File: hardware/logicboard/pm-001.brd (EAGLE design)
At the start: 45 x 45 mm, 18 parts, among them K1 G5V1, T1 2SC1815

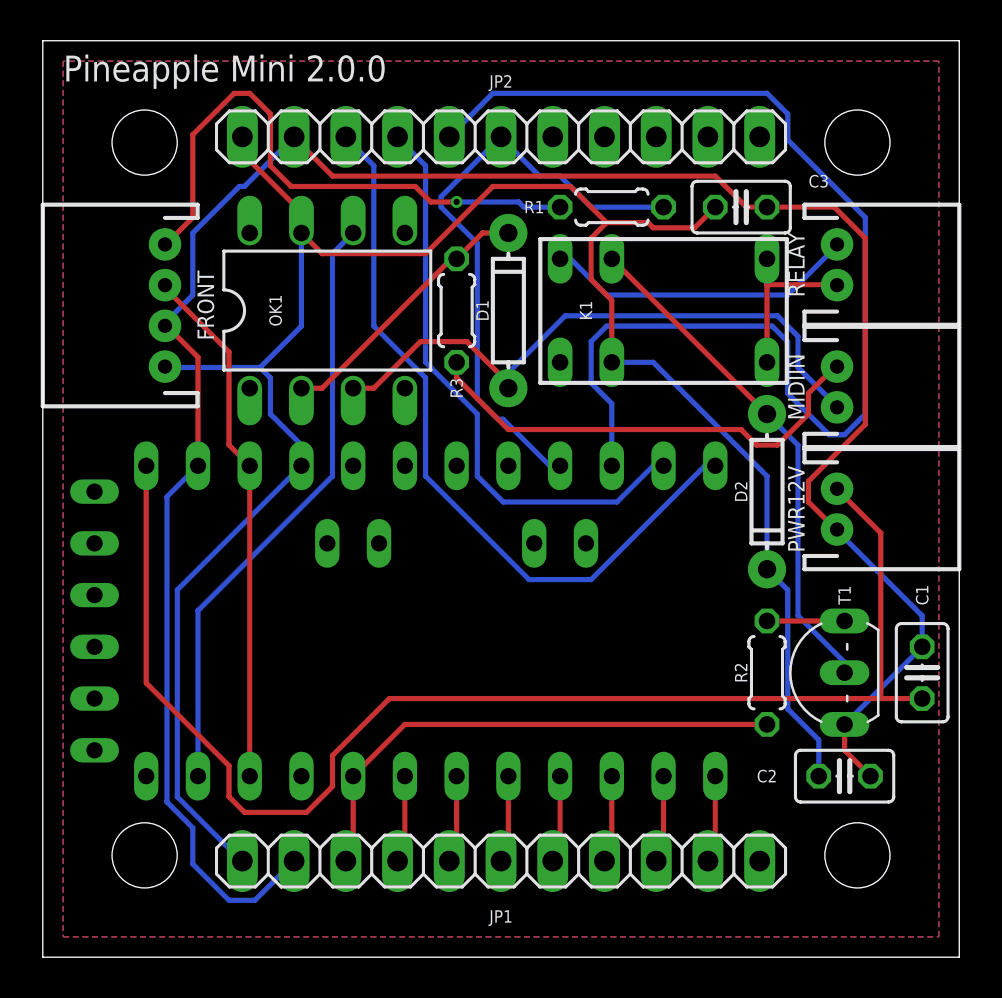
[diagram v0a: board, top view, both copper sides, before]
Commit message: Moved FTDI connector to stackable position.
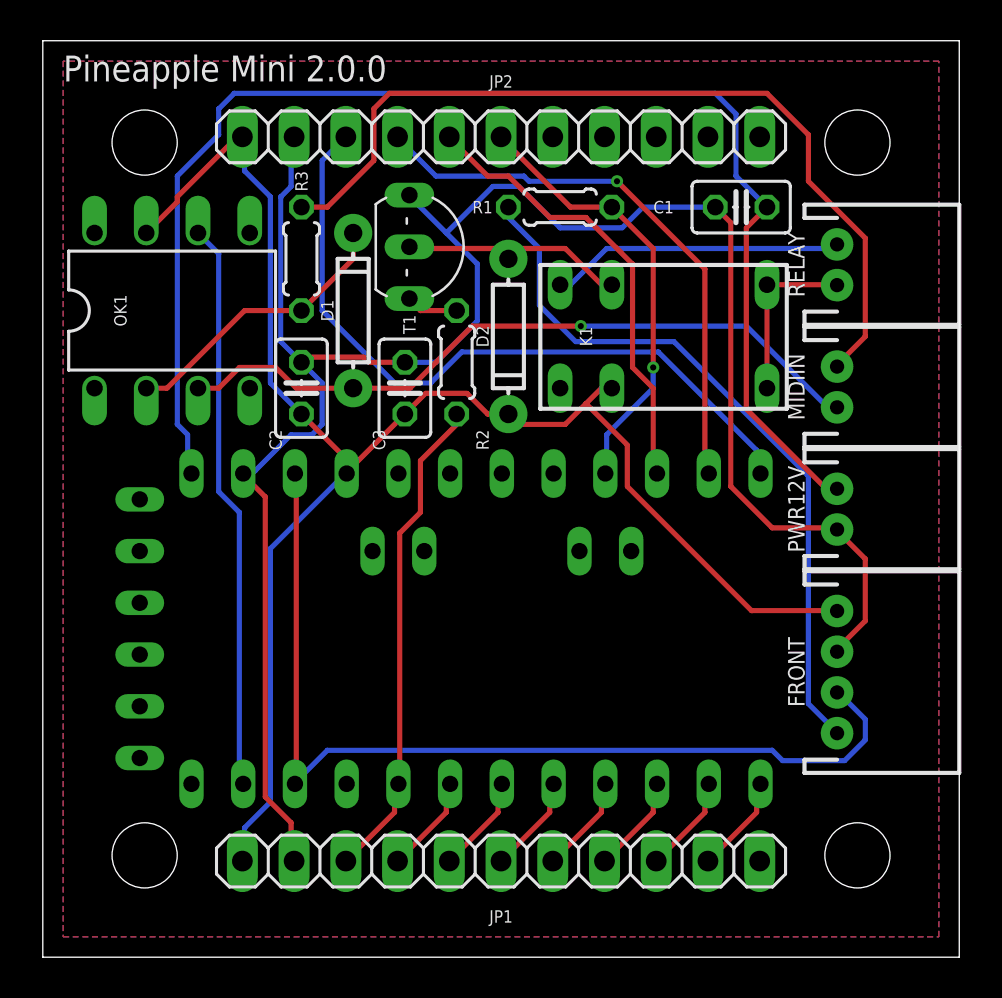
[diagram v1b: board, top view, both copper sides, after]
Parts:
- moved FRONT 37.6 mm to (39.0, 14.0), turned to 270 degrees
- moved C2 32.8 mm to (12.7, 27.9), turned to 90 degrees
- moved T1 29.9 mm to (18.0, 34.9), turned to 270 degrees
- moved C1 24.5 mm to (34.3, 36.8), turned to 180 degrees
- moved R2 21.6 mm to (20.3, 29.2)
- moved C3 18.8 mm to (17.8, 27.9), turned to 90 degrees
- moved D2 14.8 mm to (22.9, 30.5)
- moved R3 8.03 mm to (12.7, 34.3), turned to 90 degrees
- moved OK1 7.62 mm to (6.35, 31.8)
- moved D1 7.62 mm to (15.2, 31.8)
- moved R1 2.54 mm to (25.4, 36.8)
- moved U$1 2.25 mm to (20.0, 17.4)
- moved K1 1.27 mm to (30.5, 30.5)
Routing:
- net 10: track 58.6 -> 22.4 mm
- net VCC: track 103.7 -> 80.5 mm
- net RST: track 25.8 -> 47.6 mm
- net N$2: track 23.0 -> 42.6 mm
- net N$8: track 25.1 -> 11.2 mm
- net GND: track 109.0 -> 100.1 mm
- net 11: track 29.7 -> 21.8 mm, vias 0 -> 1
- net N$1: track 28.6 -> 35.3 mm, vias 1 -> 0
- net N$5: track 30.5 -> 35.1 mm, vias 0 -> 1
- net N$3: track 29.8 -> 28.0 mm
- net 0: track 25.7 -> 24.2 mm
- net N$6: track 3.81 -> 2.59 mm
- net 8: track 36.9 -> 35.7 mm
- net N$11: track 15.4 -> 14.4 mm
- net 9: track 28.7 -> 27.9 mm, vias 0 -> 1
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
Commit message: Fine tuning of the position of Arduino Pro Mini.
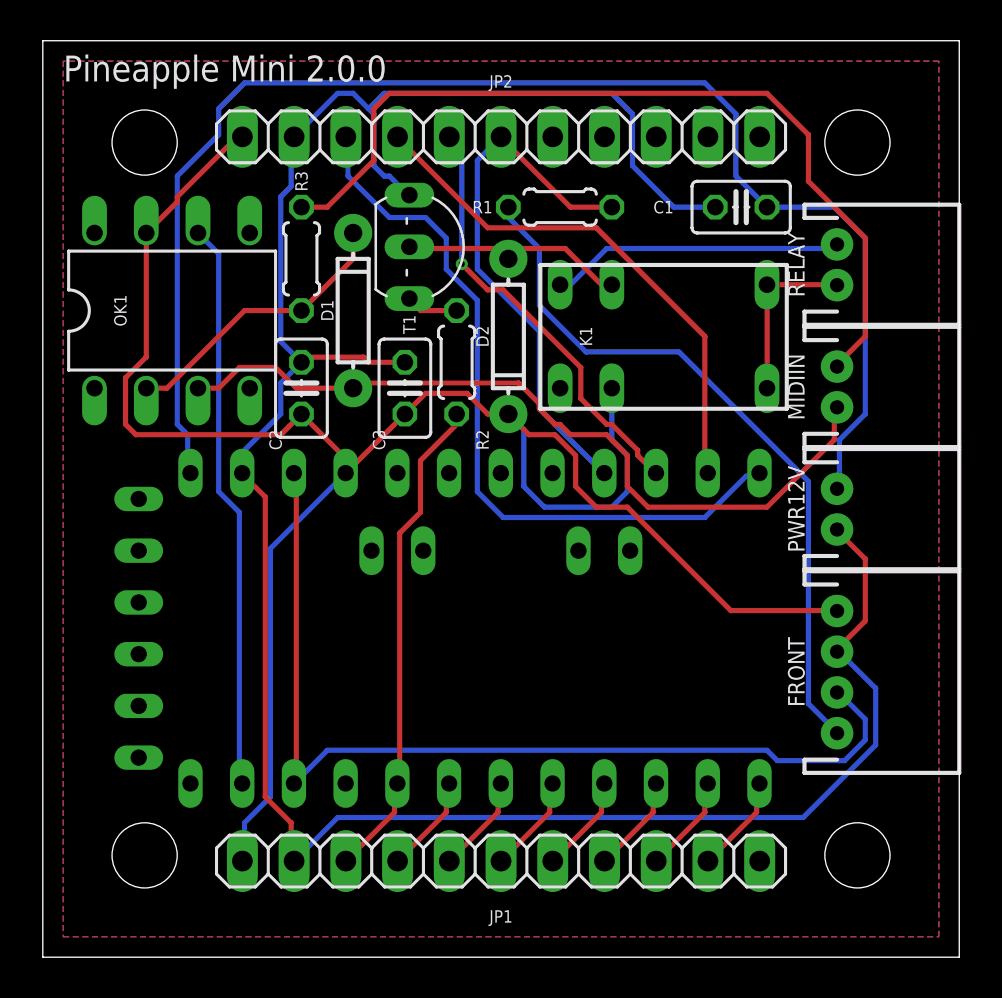
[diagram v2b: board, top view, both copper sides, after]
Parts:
- moved U$1 0.05 mm to (19.9, 17.4)
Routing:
- net GND: track 100.1 -> 118.5 mm
- net VCC: track 80.5 -> 97.1 mm
- net 11: track 21.8 -> 26.5 mm, vias 1 -> 0
- net N$5: track 35.1 -> 38.8 mm, vias 1 -> 0
- net VIN: track 66.8 -> 69.1 mm
- net 9: track 27.9 -> 25.9 mm, vias 1 -> 0
- net 10: track 22.4 -> 21.3 mm, vias 0 -> 1
- net 8: track 35.7 -> 36.4 mm

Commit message: Reversed direction of JP2.
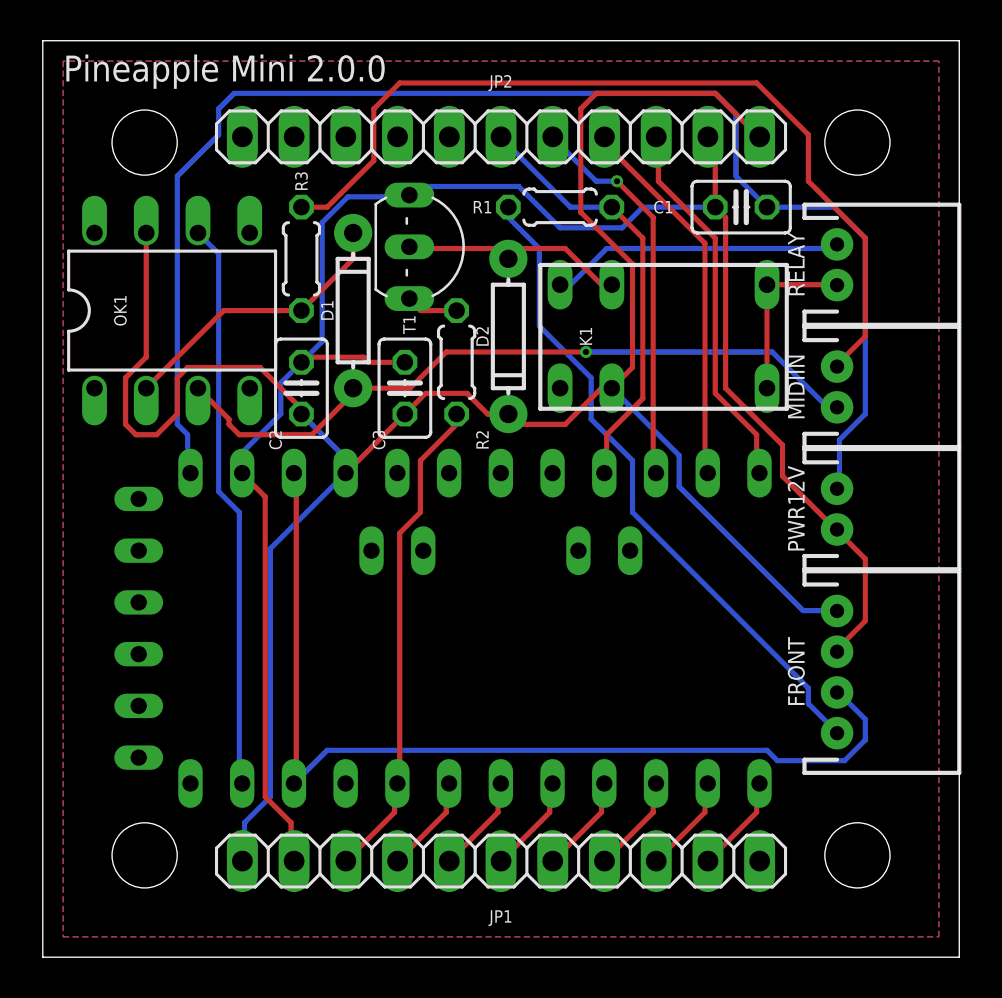
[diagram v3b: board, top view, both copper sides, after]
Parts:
- turned JP2 to 180 degrees
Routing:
- net GND: track 118.5 -> 89.7 mm
- net 8: track 36.4 -> 18.6 mm
- net VCC: track 97.1 -> 104.8 mm
- net 9: track 25.9 -> 18.7 mm
- net 11: track 26.5 -> 21.4 mm
- net N$5: track 38.8 -> 35.4 mm, vias 0 -> 1
- net N$1: track 35.2 -> 32.5 mm
- net 10: track 21.3 -> 19.2 mm
